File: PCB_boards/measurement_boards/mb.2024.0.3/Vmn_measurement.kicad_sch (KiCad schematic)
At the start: 39 parts, among them J27 Screw_Terminal_01x03, U10 DG411xJ, U2 OP07, U4 1085, U6 OP07, U7 REF03GP, U8 MCP23008-xP, U9 OP07

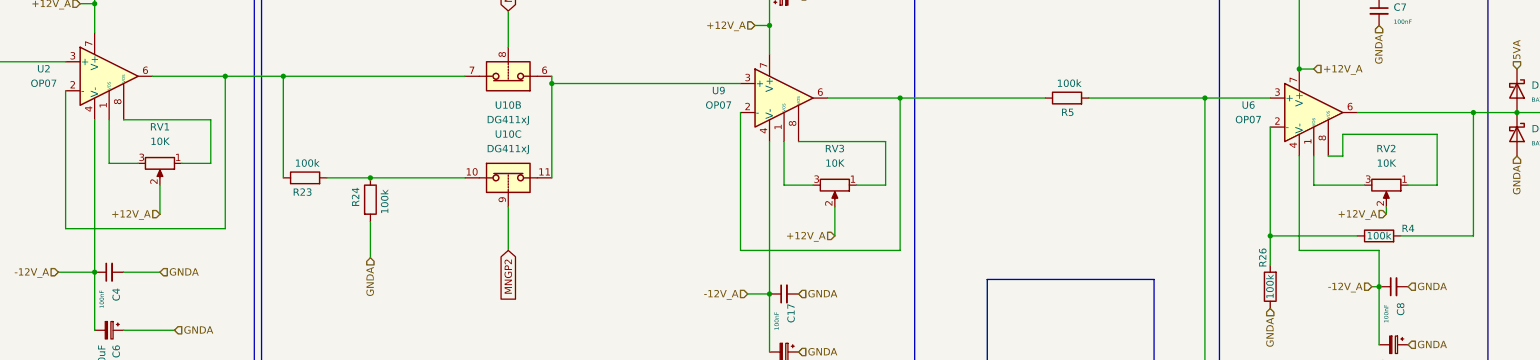
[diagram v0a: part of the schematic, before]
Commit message: last version of mesaurement board correction of web site adresse, named i2C EXT, I2C MUX and I2C Vmn, delete unused components
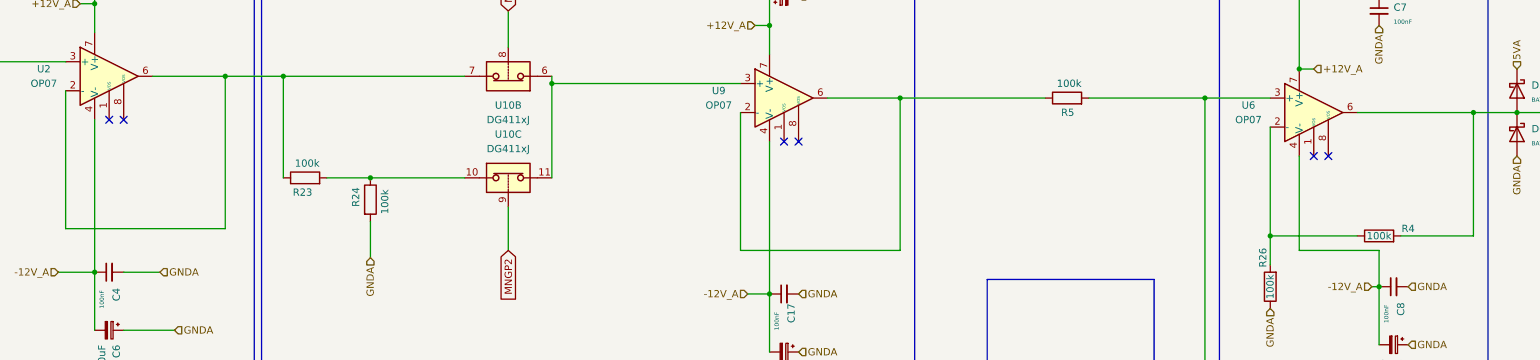
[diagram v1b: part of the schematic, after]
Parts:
- removed RV1, RV2, RV3: 10K, Potentiometer_THT:Potentiometer_Bourns_3296W_Vertical, symbol Device:R_Potentiometer
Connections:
- no-connect marks 9 -> 15
